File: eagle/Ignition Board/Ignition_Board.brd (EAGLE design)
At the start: 100 x 35.5 mm, 21 parts, among them IC1 INVERT GATES, IC2 OPTOISOLATOR, Q1 NMOSFET

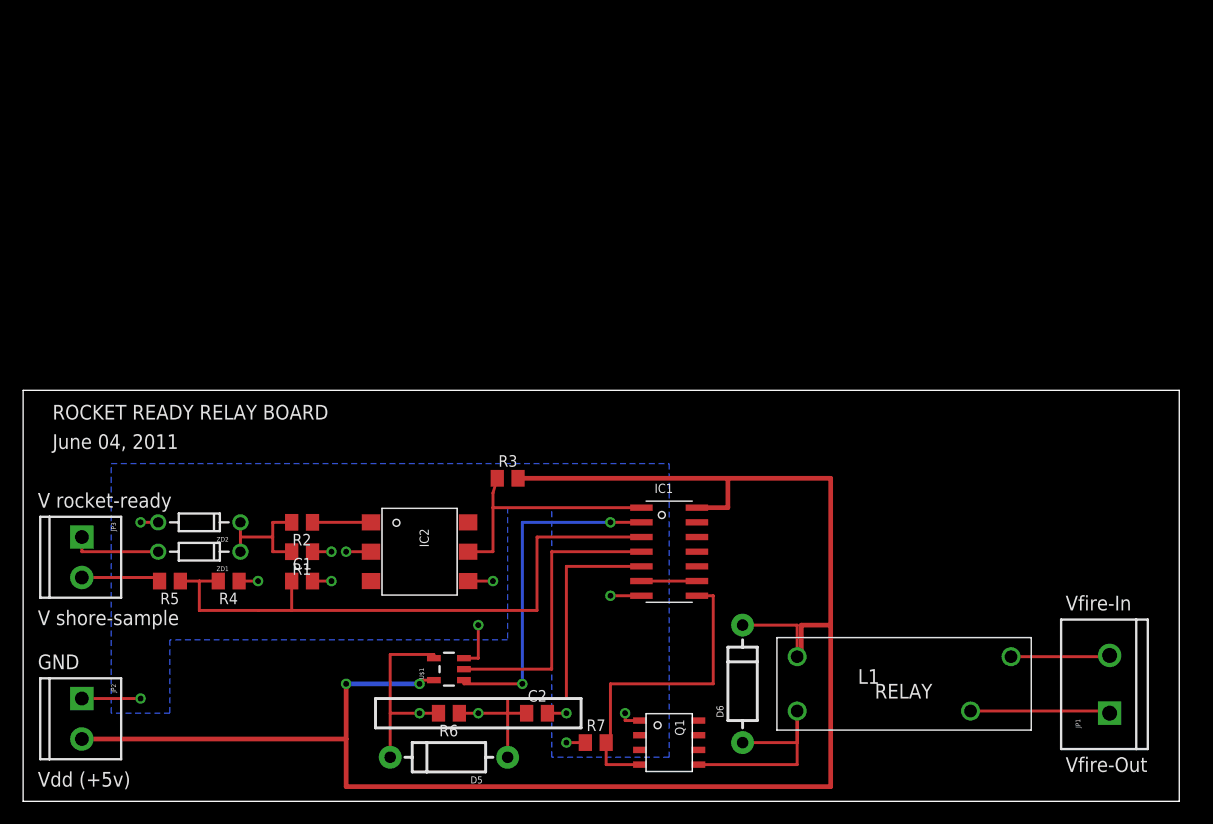
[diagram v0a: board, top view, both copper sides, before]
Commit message: Pushed latest ignition board, power board, and updated launch-tower library files. Also changed directory structure.
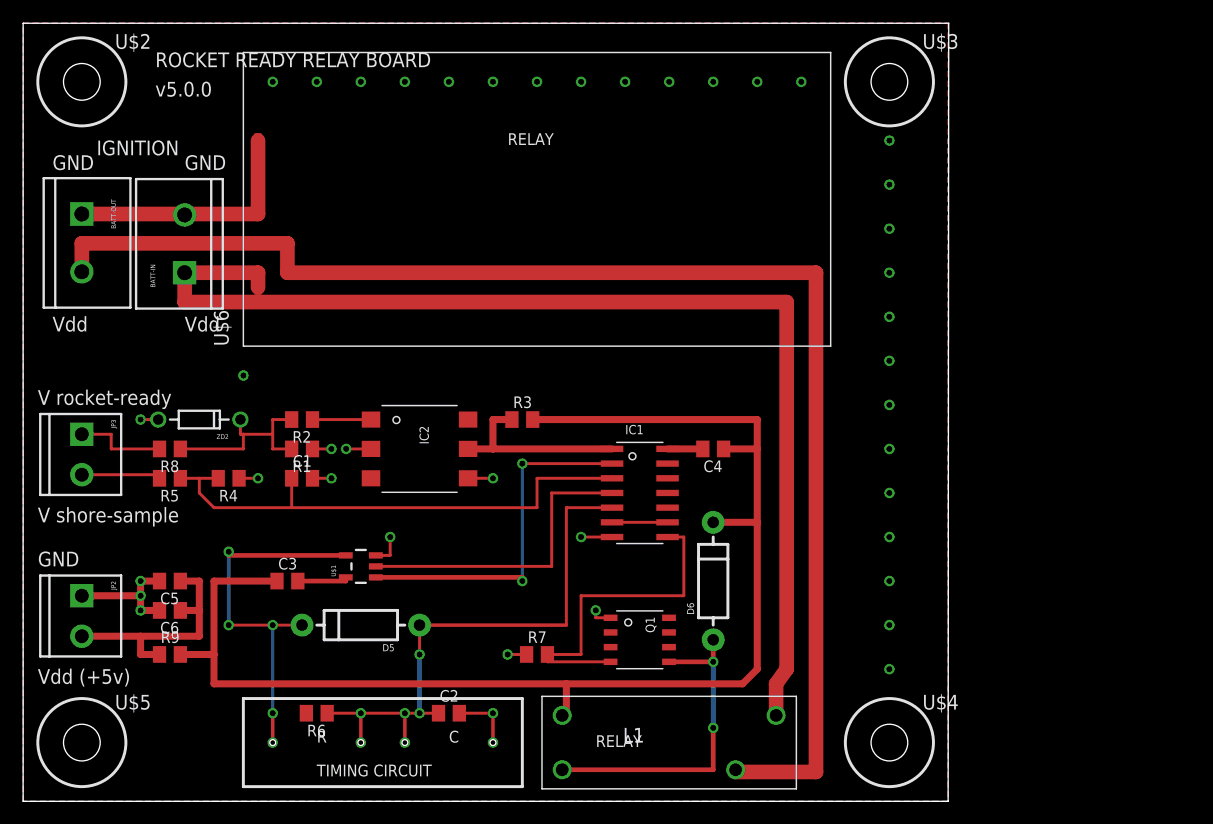
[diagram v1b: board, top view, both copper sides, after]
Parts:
- removed JP1: 5MM screw, SparkFun:SCREWTERMINAL-5MM-2
- removed ZD1: (no value), SparkFun:DIODE-ZENER
- added BATT-IN, BATT-OUT: 5MM screw, SparkFun:SCREWTERMINAL-5MM-2
- added C3, C4: (no value), rcl_custom:0805-B-NOSILK
- added C5: 10, rcl_custom:0805-B-NOSILK
- added C6: 0.01, rcl_custom:0805-B-NOSILK
- added R8: 100, rcl_custom:0805-B-NOSILK
- added R9: 0k, rcl_custom:0805-B-NOSILK
- added U$2, U$3, U$4, U$5: #4-BARE_MOUNTING_HOLE/.300, mount:#4/.300-BARE+STD_NUT_OR_STAR_WASHER
- added U$6: BATTERY, launch-tower:BATT-1
- R1: value (none) -> 4.7k
- R2: value (none) -> PICK ME
- moved L1 20.9 mm to (55.9, 5.08)
- moved D5 13.7 mm to (29.2, 15.2)
- moved U$1 11.7 mm to (29.2, 20.3)
- moved R6 11.4 mm to (25.4, 7.62)
- moved D6 9.25 mm to (59.7, 19.1)
- moved Q1 9.25 mm to (53.3, 14.0)
- moved R7 9.16 mm to (44.5, 12.7)
- moved R2 8.89 mm to (24.1, 33.0)
- moved ZD2 8.89 mm to (15.2, 33.0)
- moved C1 8.89 mm to (24.1, 27.9)
- moved IC2 8.89 mm to (34.3, 30.5)
- moved JP2 8.89 mm to (5.08, 17.8)
- moved JP3 8.89 mm to (5.08, 31.8)
- moved R1 8.89 mm to (24.1, 30.5)
- moved R4 8.89 mm to (17.8, 27.9)
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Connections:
- net N-NOT1 renamed N$15
- removed net VFIRE-IN: JP1.2, L1.SW2
- removed net VFIRE-OUT: JP1.1, L1.SW1
- removed net VROCKET: JP3.1, ZD1.P$2
- new net GND-BATT: BATT-IN.2, BATT-OUT.1, U$6.GND
- new net N$11: C3.2, U$1.5
- new net N$4: JP3.1, R8.2
- new net ROCKET-READY: R1.2, R2.2, R8.1, ZD2.P$1
- new net VCC-BATT: BATT-IN.1, BATT-OUT.2, L1.SW1, L1.SW2, U$6.VCC
- new net VDD: C3.1, C4.1, D6.C, L1.COUT, R3.2, R9.2
- net GND: now also C5.2, C6.2
- net N$12: now also C5.1, C6.1, R9.1; no longer D6.C, IC1.14, L1.COUT, R3.2, U$1.5
- net N$8: now also C4.2, IC1.14; no longer R1.2, R2.2, ZD1.P$1, ZD2.P$1
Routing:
- net VCC-BATT: track 0.00 -> 217.1 mm
- net N$12: track 153.4 -> 21.4 mm, vias 2 -> 0
- net VDD: track 0.00 -> 115.6 mm
- net GND-BATT: track 0.00 -> 21.7 mm
- net ROCKET-READY: track 0.00 -> 16.6 mm
- net N$13: track 16.8 -> 33.3 mm, vias 1 -> 5
- net N$15: track 33.9 -> 49.1 mm, vias 1 -> 6
- net VFIRE-OUT: track 12.1 -> 0.00 mm
- net GND: track 27.4 -> 36.2 mm, vias 11 -> 42
- net VFIRE-IN: track 8.58 -> 0.00 mm
- net N$8: track 11.2 -> 3.05 mm
- net N$4: track 0.00 -> 7.99 mm, vias 1 -> 0
- net VROCKET: track 7.87 -> 0.00 mm
- net N$9: track 20.6 -> 28.1 mm, vias 0 -> 2
- net N$7: track 52.9 -> 45.9 mm
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- added copper zone on layer 1, net GND
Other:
- board size 100 x 35.5 mm -> 80.1 x 67.3 mm
- board text added: "C"
- board text added: "IGNITION"
- board text added: "R"
- board text added: "TIMING CIRCUIT"
- board text added: "Vdd"
- board text added: "v5.0.0"
- board text removed: "June 04, 2011"
- board text removed: "Vfire-In"
- board text removed: "Vfire-Out"
